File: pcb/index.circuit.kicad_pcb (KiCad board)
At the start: 4 copper layers, 91 x 68 mm, 42 parts, among them J1 TYPE_C_31_M_12, U1 RP2040, U2 W25Q16JVSSIQ, U3 AP2112K_3_3TRG1, Y1 X322512MSB4SI

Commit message: pcb: fabricable 4-layer route — NPTH keepouts, GND/V3V3 planes, RP2040 pour
The prior route was not fabricable: 11 signal traces crossed keyswitch/USB
mounting holes (open nets), GND/V3V3 snaked as ~250 tracks on the signal
layers, and two decaps were floating (top pad, back-layer traces, no via).
Re-routed through a corrected pipeline; final DRC is clean (0 shorts /
0 crossings / 0 unconnected / 0 courtyard overlaps).

Routing pipeline (scripts/route4.sh):
- add_npth_keepouts.py: keepout every non-plated mechanical hole (keyswitch
  poles/pins, USB posts, screw holes) so no trace crosses a drilled hole —
  add_cutout_keepouts.py only covers Edge.Cuts, not pad-holes.
- keep GND/V3V3 in the route (fine-pitch QFN pins need routed dogbones that
  only the autorouter places), pour In1=GND / In2=V3V3 inner planes.
- fix_ldo_planes.py + collision-aware fanout_planes.py (via-in-pad first):
  convert the dense LDO/USB power corner to plane-vias without shorting.
- add_local_zone.py: local GND pour over the RP2040 (U1) so its ground pins
  tie into copper on their own layer.
- apply_fab_rules.py: JLCPCB design rules (0.127 mm clearance, 0.6/0.3 vias).

New tooling: check_floating.py (wrong-side/floating SMD-pad detector),
add_npth_keepouts.py, add_local_zone.py, add_dsn_planes.py, fix_ldo_planes.py,
patch_stragglers.py, apply_fix.sh (single-call kipy/IPC runner), plus
inspect_pads / finish_converge / stitch_planes helpers.

Regenerated: JLCPCB+PCBWay fab bundle, PCBA GLB, routed-board render (0004).

Co-Authored-By: Claude Opus 4.8 (1M context) <noreply@anthropic.com>
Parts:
- moved SW_RST 61.8 mm to (136.0, 127.0)
- moved SW_BOOT 60.8 mm to (136.0, 117.0)
- moved C_IN 16.0 mm to (108.0, 129.0)
- moved U3 12.0 mm to (116.0, 129.0)
- moved C_OUT 9.00 mm to (124.0, 129.0)
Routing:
- net V3V3: track 186.6 -> 130.0 mm, vias 7 -> 8
- net GND: track 406.3 -> 353.9 mm, vias 7 -> 8
- net RUN: track 102.2 -> 80.7 mm, vias 2 -> 1
- net DVDD: track 18.1 -> 34.6 mm, vias 1 -> 2
- net USB_DP: track 26.2 -> 33.8 mm, vias 0 -> 2
- net USB_DM: track 23.8 -> 31.1 mm, vias 0 -> 2
- net QSPI_SCLK: track 11.0 -> 17.5 mm
- net XIN: track 22.0 -> 16.4 mm, vias 1 -> 2
- net QSPI_SD2: track 23.2 -> 18.5 mm
- net KEY3: track 66.7 -> 62.1 mm, vias 1 -> 0
- net SHIFT: track 35.6 -> 39.4 mm
- net QSPI_SD3: track 16.2 -> 19.9 mm
- net KEY5: track 50.2 -> 46.8 mm
- net LED_DIN: track 31.0 -> 27.8 mm
- net BOOT_BTN: track 59.3 -> 56.1 mm, vias 0 -> 1
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- added copper zone on F.Cu, net GND
- removed copper zone on F.Cu, net VBUS

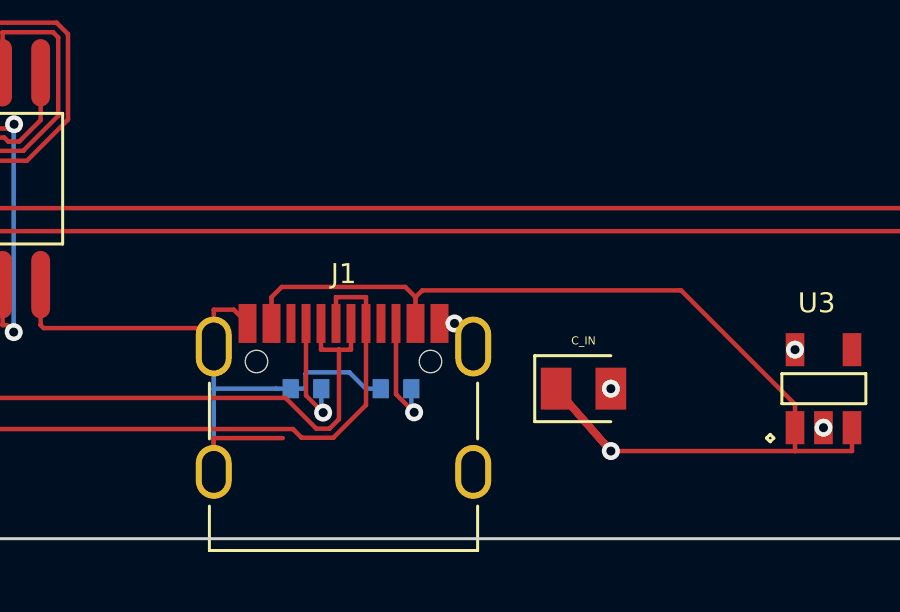
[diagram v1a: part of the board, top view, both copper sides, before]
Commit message: pcb: fix JLC DFM hole-spacing — reroute J1.14 ground fanout off the mount hole
JLCPCB DFM flagged a plated-hole spacing danger: a GND fanout via sat 0.041 mm
from J1's 1.6 mm USB-C mounting hole (< the 0.5 mm hole-to-hole minimum).
J1.14 (SMD ground pad) now fans out through a via placed clear of both the
mount hole and the VBUS trace; closest non-connector hole spacing is 0.537 mm.
DRC stays clean (0 shorts / 0 unconnected). Regenerated fab bundle.

New helpers: fix_hole_spacing.py (delete finisher vias too close to a hole),
reconnect_j14.py (re-fanout a pad clear of holes + copper). Note: kipy's
get_tracks() does NOT return vias — must use get_vias().

Remaining DFM items are non-blocking: J1's own 0.335 mm mount-post-to-pad
spacing (part of the qualified USB-C footprint) and silkscreen-over-pad/hole +
sub-0.15 mm silk (cosmetic; JLC auto-clips silk around openings).

Co-Authored-By: Claude Opus 4.8 (1M context) <noreply@anthropic.com>
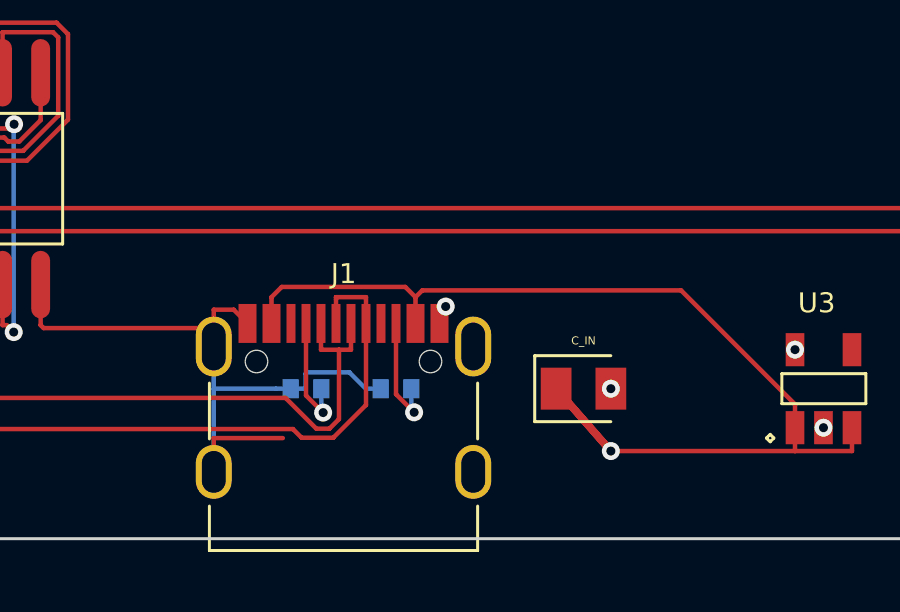
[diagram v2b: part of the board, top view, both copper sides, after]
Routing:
- net GND: track 353.9 -> 354.5 mm
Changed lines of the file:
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@@
+	)
+	(segment
+		(start 103.200006 126.825856)
+		(end 103.405218 126.26204)
+		(width 0.2)
+		(layer "F.Cu")
+		(net 13)
 	)
 	(segment
@@
 	)
 	(via
-		(at 103.700006 126.825856)
+		(at 103.405218 126.26204)
 		(size 0.6)
 		(drill 0.3)
